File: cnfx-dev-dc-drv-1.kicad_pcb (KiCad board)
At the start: 2 copper layers, 51.3 x 51.3 mm, 67 parts, among them J1 Conn_01x03, J2 TC2030, J3 Conn_01x02, J4 Conn_01x02, J6 Conn_01x04_Pin, J7 Conn_01x02, J8 Conn_01x02, SW1 SW_Push, SW2 SW_Push, SW3 SW_Push, U1 SN65HVD230, U2 TPS259472A, U3 HT753-1, U4 STM32F103C8Tx, U5 DRV8837, U6 DRV8837, Y1 8M

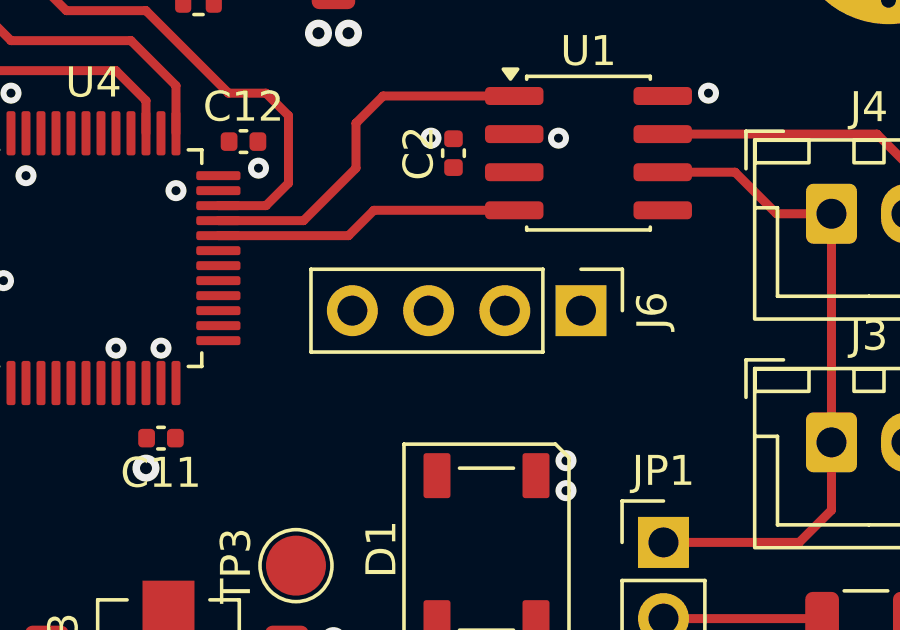
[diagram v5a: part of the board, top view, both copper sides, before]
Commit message: pcb: add UART routing
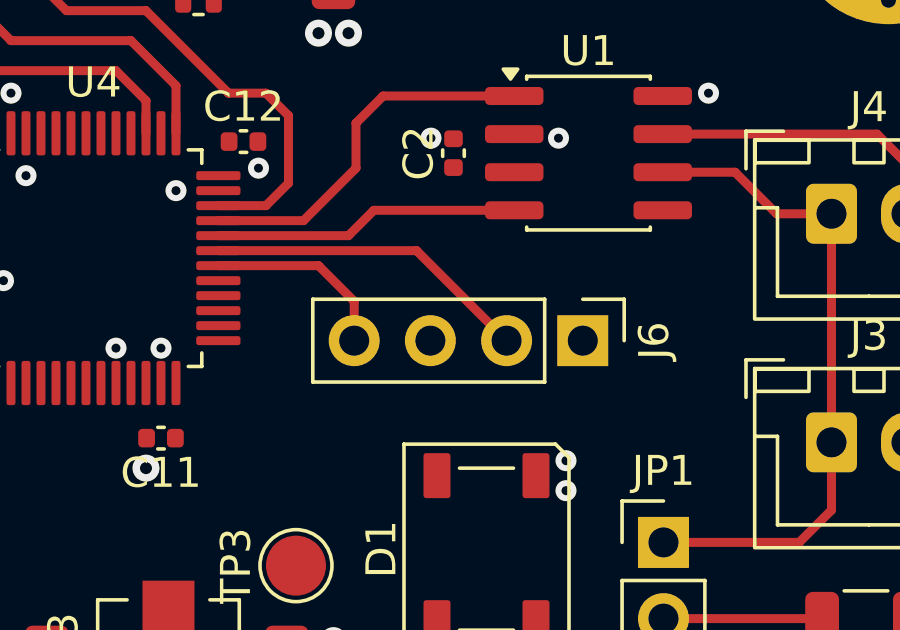
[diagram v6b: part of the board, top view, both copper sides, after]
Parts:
- moved J6 1.00 mm to (129.8, 73.8)
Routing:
- net /U0RXD: track 0.00 -> 10.9 mm
- net /U0TXD: track 0.00 -> 6.33 mm
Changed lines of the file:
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@@
 	(footprint "Connector_PinHeader_2.54mm:PinHeader_1x04_P2.54mm_Vertical"
 		(layer "F.Cu")
-		(at 129.75 72.75 -90)
+		(at 129.81 73.75 -90)
 		(descr "Through hole straight pin header, 1x04, 2.54mm pitch, single row")
 		(tags "Through hole pin header THT 1x04 2.54mm single row")
@@
 	)
 	(segment
+		(start 124.27 70.75)
+		(end 117.6625 70.75)
+		(width 0.3)
+		(layer "F.Cu")
+		(net "/U0RXD")
+	)
+	(segment
+		(start 127.27 73.75)
+		(end 124.27 70.75)
+		(width 0.3)
+		(layer "F.Cu")
+		(net "/U0RXD")
+	)
+	(segment
+		(start 117.6625 71.25)
+		(end 121 71.25)
+		(width 0.3)
+		(layer "F.Cu")
+		(net "/U0TXD")
+	)
+	(segment
+		(start 121 71.25)
+		(end 122.19 72.44)
+		(width 0.3)
+		(layer "F.Cu")
+		(net "/U0TXD")
+	)
+	(segment
+		(start 122.19 72.44)
+		(end 122.19 73.75)
+		(width 0.3)
+		(layer "F.Cu")
+		(net "/U0TXD")
+	)
+	(segment

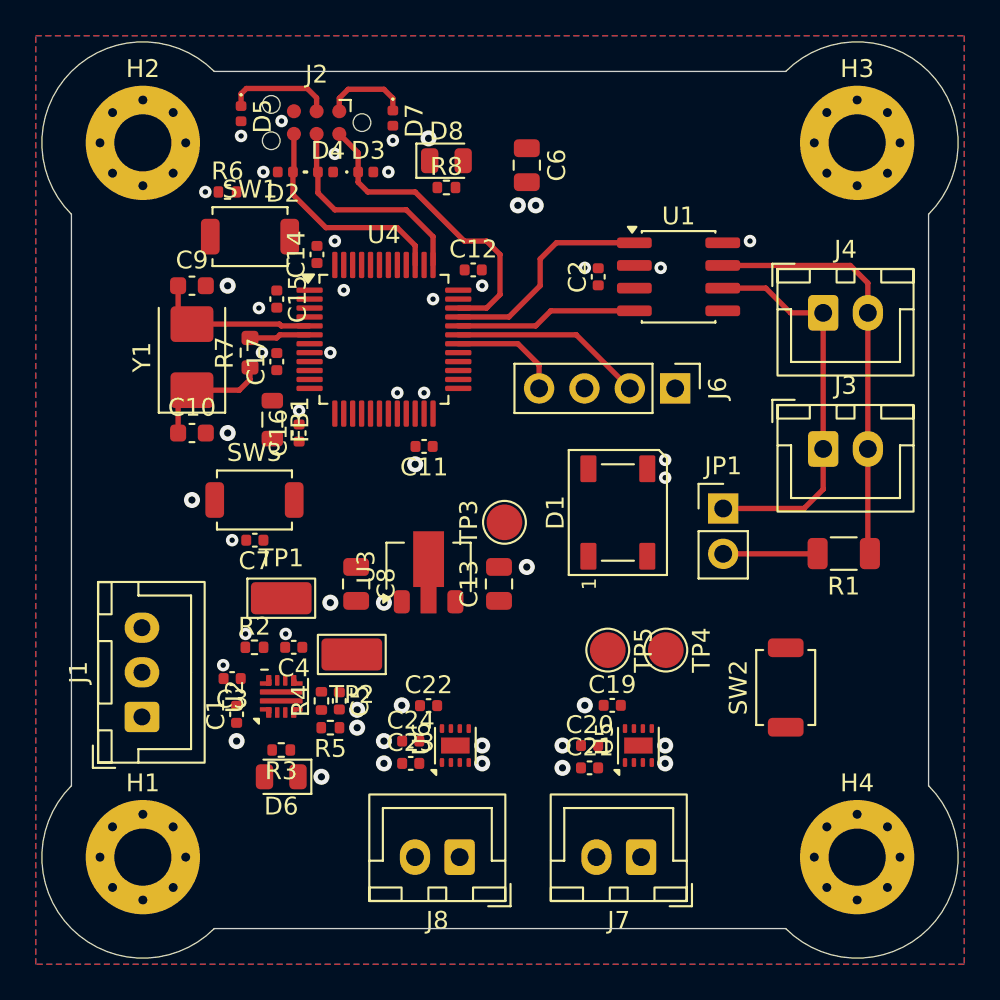
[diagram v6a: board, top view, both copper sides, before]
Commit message: pcb: add DC drivers routing
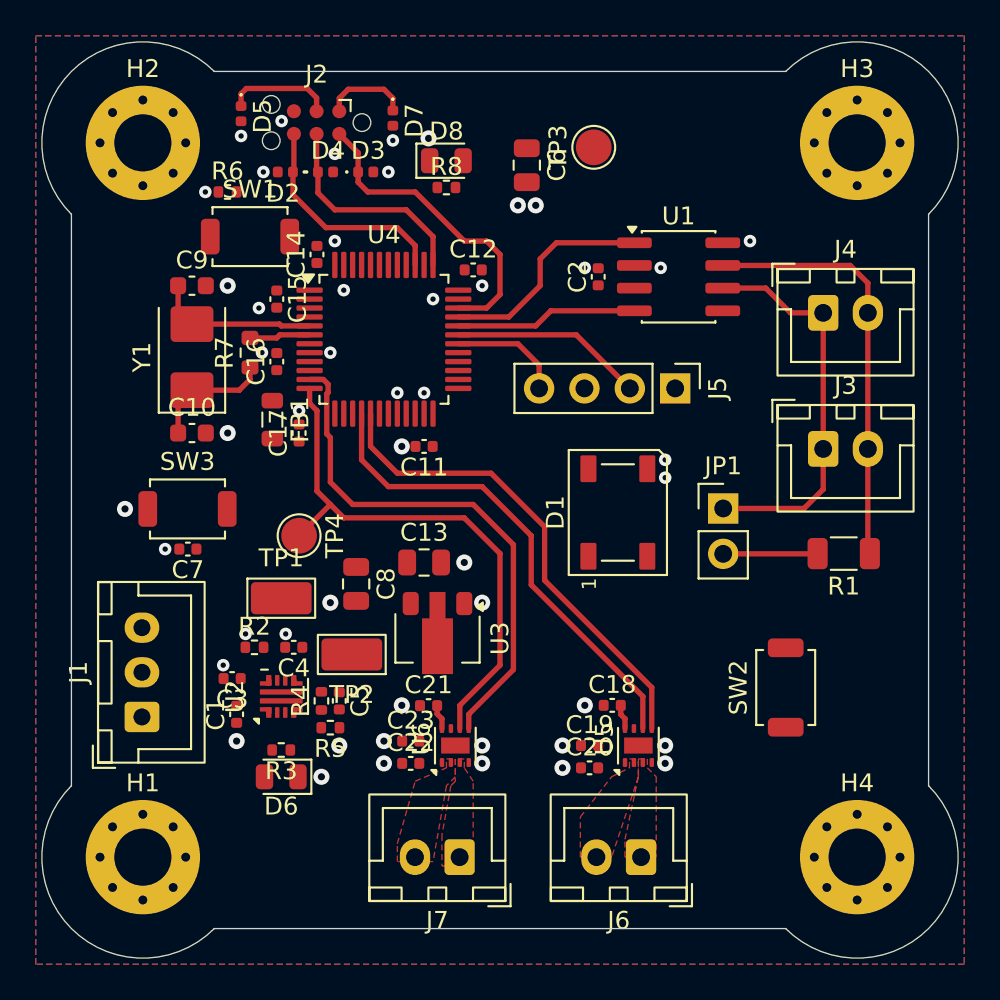
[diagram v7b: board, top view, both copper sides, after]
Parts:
- removed TP5: TestPoint, TestPoint:TestPoint_Pad_D2.0mm
- moved TP3 21.6 mm to (125.2, 60.2)
- moved TP4 21.5 mm to (108.8, 82.0)
- moved C13 4.36 mm to (115.8, 83.5), turned to 0 degrees
- moved U3 4.03 mm to (116.5, 87.8), turned to -90 degrees
- moved C7 3.78 mm to (102.5, 82.8)
- moved SW3 3.78 mm to (102.5, 80.5)
- renumbered C17 to C16, C16 to C17, C19 to C18, C20 to C19, C21 to C20, C22 to C21, C23 to C22, C24 to C23, J6 to J5, J7 to J6, J8 to J7
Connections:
- TP4 pad 1: /DC Driver/IN2 -> /DC Driver 2/IN1
- U4 pad 10: /DC Driver/~{SLEEP} -> /DC Driver 2/~{SLEEP}
- U4 pad 11: /DC Driver/IN1 -> /DC Driver 2/IN2
- U4 pad 12: /DC Driver/IN2 -> /DC Driver 2/IN1
- U4 pad 15: /DC Driver 2/~{SLEEP} -> /DC Driver/~{SLEEP}
- U4 pad 16: /DC Driver 2/IN1 -> /DC Driver/IN1
- U4 pad 17: /DC Driver 2/IN2 -> /DC Driver/IN2
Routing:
- net /DC Driver 2/IN1: track 0.00 -> 30.8 mm
- net /DC Driver 2/IN2: track 0.00 -> 29.8 mm
- net /DC Driver/IN2: track 0.00 -> 27.2 mm
- net /DC Driver/IN1: track 0.00 -> 27.2 mm
- net +3V3: track 4.83 -> 7.63 mm
- net GND: vias 50 -> 49
- added copper zone on F.Cu, net Net-(J6-Pin_1)
- added copper zone on F.Cu, net Net-(J6-Pin_2)
- added copper zone on F.Cu, net Net-(J7-Pin_1)
- added copper zone on F.Cu, net Net-(J7-Pin_2)

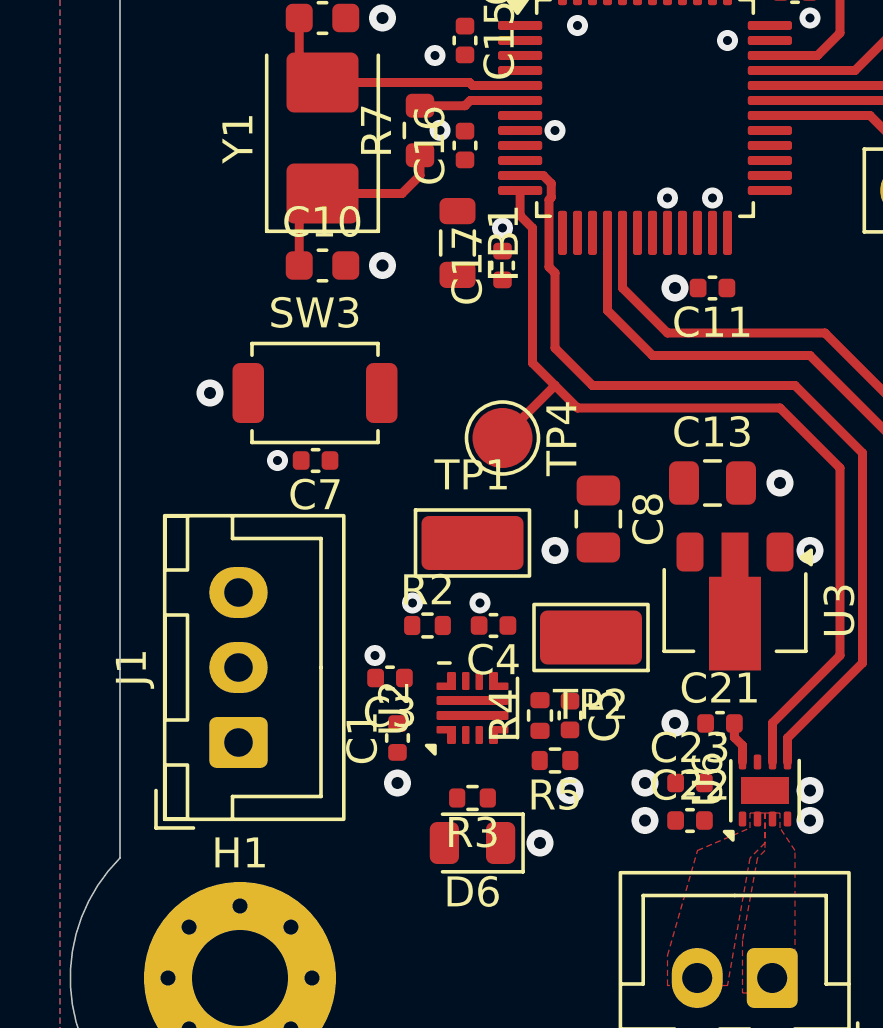
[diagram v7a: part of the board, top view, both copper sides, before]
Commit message: pcb: add efuse routing
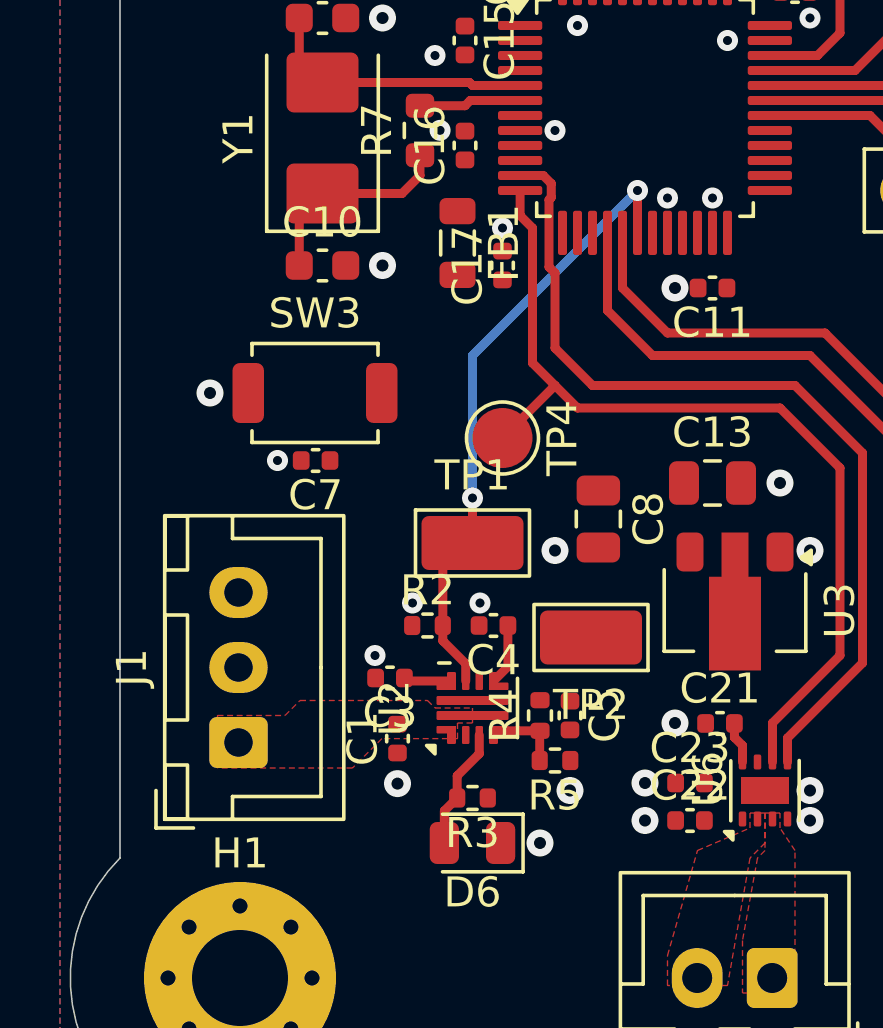
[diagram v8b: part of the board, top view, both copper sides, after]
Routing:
- net /ILM: track 0.00 -> 20.9 mm, vias 0 -> 2
- net Net-(D6-A): track 0.00 -> 4.08 mm
- net Net-(U2-PGTH): track 0.00 -> 2.60 mm
- net Net-(U2-DVDT): track 0.00 -> 2.05 mm
- net Net-(U2-ITIMER): track 0.00 -> 1.61 mm
- added copper zone on F.Cu, net +5V_IN
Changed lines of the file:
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@@
 	(footprint "Capacitor_SMD:C_0402_1005Metric"
 		(layer "F.Cu")
-		(at 105.25 92 90)
+		(at 105.25 92.02 90)
 		(descr "Capacitor SMD 0402 (1005 Metric), square (rectangular) end terminal, IPC-7351 nominal, (Body size source: IPC-SM-782 page 76, https://www.pcb-3d.com/wordpress/wp-content/uploads/ipc-sm-782a_amendment_1_and_2.pdf)")
 		(tags "capacitor")
@@
 	)
 	(via
-		(at 105.25 93.5)
+		(at 105.25 93.52)
 		(size 0.9)
 		(drill 0.4)
@@
 	)
 	(segment
+		(start 107.05 90.1)
+		(end 105.58 90.1)
+		(width 0.3)
+		(layer "F.Cu")
+		(net "Net-(U2-ITIMER)")
+	)
+	(segment
+		(start 105.58 90.1)
+		(end 105.48 90)
+		(width 0.3)
+		(layer "F.Cu")
+		(net "Net-(U2-ITIMER)")
+	)
+	(segment
+		(start 108.93 88.25)
+		(end 108.93 89.62)
+		(width 0.3)
+		(layer "F.Cu")
+		(net "Net-(U2-DVDT)")
+	)
+	(segment
+		(start 108.93 89.62)
+		(end 108.45 90.1)
+		(width 0.3)
+		(layer "F.Cu")
+		(net "Net-(U2-DVDT)")
+	)
+	(segment
 		(start 109.2037 56.9537)
 		(end 105.7963 56.9537)
@@
 	)
 	(segment
+		(start 106.8125 95.5)
+		(end 106.8125 94.4275)
+		(width 0.3)
+		(layer "F.Cu")
+		(net "Net-(D6-A)")
+	)
+	(segment
+		(start 106.8125 94.4275)
+		(end 107.24 94)
+		(width 0.3)
+		(layer "F.Cu")
+		(net "Net-(D6-A)")
+	)
+	(segment
+		(start 107.24 94)
+		(end 107.24 93.26)
+		(width 0.3)
+		(layer "F.Cu")
+		(net "Net-(D6-A)")
+	)
+	(segment
+		(start 107.24 93.26)
+		(end 107.975 92.525)
+		(width 0.3)
+		(layer "F.Cu")
+		(net "Net-(D6-A)")
+	)
+	(segment
+		(start 107.975 92.525)
+		(end 107.975 91.9)
+		(width 0.3)
+		(layer "F.Cu")
+		(net "Net-(D6-A)")
+	)
+	(segment
 		(start 140.6 69.52)
 		(end 140.6 77.14)
@@
 	)
 	(segment
+		(start 108.59 91.76)
+		(end 108.45 91.9)
+		(width 0.3)
+		(layer "F.Cu")
+		(net "Net-(U2-PGTH)")
+	)
+	(segment
+		(start 109.99 91.77)
+		(end 110 91.76)
+		(width 0.3)
+		(layer "F.Cu")
+		(net "Net-(U2-PGTH)")
+	)
+	(segment
+		(start 110 91.76)
+		(end 108.59 91.76)
+		(width 0.3)
+		(layer "F.Cu")
+		(net "Net-(U2-PGTH)")
+	)
+	(segment
+		(start 109.99 92.75)
+		(end 109.99 91.77)
+		(width 0.3)
+		(layer "F.Cu")
+		(net "Net-(U2-PGTH)")
+	)
+	(segment
 		(start 106 70.925)
 		(end 107.5 70.925)
@@
 		(net "/DC Driver/IN1")
 	)
+	(segment
+		(start 106.76 86.24)
+		(end 107 86)
+		(width 0.3)
+		(layer "F.Cu")
+		(net "/ILM")
+	)
+	(segment
+		(start 113.25 73.75)
+		(end 113.25 75.1625)
+		(width 0.3)
+		(layer "F.Cu")
+		(net "/ILM")
+	)
+	(segment
+		(start 106.76 88.25)
+		(end 106.76 86.24)
+		(width 0.3)
+		(layer "F.Cu")
+		(net "/ILM")
+	)
+	(segment
+		(start 107.525 90.1)
+		(end 107.525 89.525)
+		(width 0.3)
+		(layer "F.Cu")
+		(net "/ILM")
+	)
+	(segment
+		(start 107.75 85.5)
+		(end 107.75 84)
+		(width 0.3)
+		(layer "F.Cu")
+		(net "/ILM")
+	)
+	(segment
+		(start 106.76 88.76)
+		(end 106.76 88.25)
+		(width 0.3)
+		(layer "F.Cu")
+		(net "/ILM")
+	)
+	(segment
+		(start 107 86)
+		(end 107.25 86)
+		(width 0.3)
+		(layer "F.Cu")
+		(net "/ILM")
+	)
+	(segment
+		(start 107.525 89.525)
+		(end 106.76 88.76)
+		(width 0.3)
+		(layer "F.Cu")
+		(net "/ILM")
+	)
+	(segment
+		(start 107.25 86)
+		(end 107.75 85.5)
+		(width 0.3)
+		(layer "F.Cu")
+		(net "/ILM")
+	)
+	(via
+		(at 113.25 73.75)
+		(size 0.7)
+		(drill 0.3)
+		(layers "F.Cu" "B.Cu")
+		(net "/ILM")
+	)
+	(via
+		(at 107.75 84)
+		(size 0.7)
+		(drill 0.3)
+		(layers "F.Cu" "B.Cu")
+		(net "/ILM")
+	)
+	(segment
+		(start 107.75 79.25)
+		(end 113.25 73.75)
+		(width 0.3)
+		(layer "B.Cu")
+		(net "/ILM")
+	)
+	(segment
+		(start 107.75 84)
+		(end 107.75 79.25)
+		(width 0.3)
+		(layer "B.Cu")
+		(net "/ILM")
+	)
+	(zone
+		(net "+5V_IN")
+		(layer "F.Cu")
+		(hatch edge 0.5)
+		(priority 5)
+		(connect_pads yes
+			(clearance 0.2)
+		)
+		(min_thickness 0.15)
+		(fill yes
+			(thermal_gap 0.5)
+			(thermal_bridge_width 0.5)
+			(island_removal_mode 0)
+		)
+		(polygon
+			(pts
+				(xy 99.25 91.25) (xy 101.5 91.25) (xy 102 90.75) (xy 106.25 90.75) (xy 106.5 91) (xy 107.75 91)
+				(xy 107.75 91.5) (xy 107.25 91.5) (xy 107.25 92.02) (xy 104.73 92.02) (xy 103.75 93) (xy 99.25 93)
+			)
+		)
+	)
 	(zone
